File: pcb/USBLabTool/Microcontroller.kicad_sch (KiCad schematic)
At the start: 19 parts, among them J1 Conn_01x06_Pin, J2 Conn_02x12_Odd_Even, SW1 TS02-66-73-BK-100-SCR-D, U12 STM32H562VGTx, Y1 32.768kHz, Y2 NX2016SA-25M-EXS00A-CS08742

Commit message: fixes
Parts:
- added JP6, JP7: SJ, Jumper:SolderJumper-2_P1.3mm_Open_RoundedPad1.0x1.5mm, symbol Jumper:SolderJumper_2_Open
- added R82, R83: 0, Resistor_SMD:R_0603_1608Metric_Pad0.98x0.95mm_HandSolder, symbol Device:R
- added R84, R85: 5.1k, Resistor_SMD:R_0603_1608Metric_Pad0.98x0.95mm_HandSolder, symbol Device:R
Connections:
- net RCC_OSC32_IN: now also R82.1; no longer C35.2, Y1.2
- net RCC_OSC32_OUT: now also R83.1; no longer C36.2, Y1.1
- net RCC_OSC_IN: now also JP6.1 (A); no longer C33.1, Y2.1
- net RCC_OSC_OUT: now also JP7.2 (B); no longer C34.2, Y2.3
- net UCPD_CC1: now also R84.2; no longer U12.52 (PB13)
- net UCPD_CC2: now also R85.2; no longer U12.53 (PB14)
- net USB_D+ renamed USB_FS_P
- net USB_D- renamed USB_FS_N
- new net: R85.1, U12.53 (PB14)
- new net: C34.2, JP7.1 (A), Y2.3
- new net: C33.1, JP6.2 (B), Y2.1
- new net: C36.2, R83.2, Y1.1
- new net: C35.2, R82.2, Y1.2
- new net: R84.1, U12.52 (PB13)
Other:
- moved on the sheet: C35, C36, Y1

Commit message: V2 fixed
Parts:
- added JP8, JP9: SJ, Jumper:SolderJumper-2_P1.3mm_Open_RoundedPad1.0x1.5mm, symbol Jumper:SolderJumper_2_Open
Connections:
- net RCC_OSC32_IN: now also JP8.1 (A); no longer R82.1
- net RCC_OSC32_OUT: now also JP9.1 (A); no longer R83.1
- new net: JP9.2 (B), R83.1
- new net: JP8.2 (B), R82.1
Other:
- moved on the sheet: R83

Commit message: PCB V2 updates
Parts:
- removed CR2: ESDALC6V1-1U2, userfp:DIODE_ESDALC6V1-1U2_STM, symbol USBLabTool:ESDALC6V1-1U2
- removed JP8, JP9: SJ, Jumper:SolderJumper-2_P1.3mm_Open_RoundedPad1.0x1.5mm, symbol Jumper:SolderJumper_2_Open
- removed U12: STM32H562VGTx, Package_QFP:LQFP-100_14x14mm_P0.5mm, symbol MCU_ST_STM32H5:STM32H562VGTx
- added CR1: ESDALC6V1-1M2, Diode_SMD:D_SOD-882, symbol USBLabTool:ESDALC6V1-1M2
- added H3, H4: MountingHole, MountingHole:MountingHole_2.2mm_M2, symbol Mechanical:MountingHole
- added U12: STM32H563VITx, Package_QFP:LQFP-100_14x14mm_P0.5mm, symbol MCU_ST_STM32H5:STM32H563VITx
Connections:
- net +3.3V: now also U12.100 (VDD), U12.11 (VDD), U12.28 (VDD), U12.50 (VDD), U12.6 (VBAT), U12.73 (VDDUSB), U12.75 (VDD)
- net ADC1_INP0: now also U12.23 (PA0)
- net ADC2_INP3: now also U12.31 (PA6)
- net C0_IN: now also U12.29 (PA4)
- net C1_IN: now also U12.30 (PA5)
- net CH0_ACDC: now also U12.18 (PC3)
- net CH0_amp_1: now also U12.36 (PB1)
- net CH0_amp_10: now also U12.37 (PB2)
- net CH0_amp_2.5: now also U12.44 (PE13)
- net CH0_amp_5: now also U12.43 (PE12)
- net CH0_attenuate: now also U12.17 (PC2)
- net CH1_ACDC: now also U12.33 (PC4)
- net CH1_amp_1: now also U12.34 (PC5)
- net CH1_amp_10: now also U12.35 (PB0)
- net CH1_amp_2.5: now also U12.16 (PC1)
- net CH1_amp_5: now also U12.15 (PC0)
- net CH1_attenuate: now also U12.1 (PE2)
- net DEBUG_JTCK_SWCLK: now also U12.76 (PA14(JTCK)
- net DEBUG_JTD-SW0: now also U12.89 (PB3(JTDO)
- net DEBUG_JTMS-SWDI0: now also U12.72 (PA13(JTMS)
- net GAIN_C0: now also U12.64 (PC7)
- net GAIN_C1: now also U12.63 (PC6)
- net GND: now also CR1.2 (A), U12.10 (VSS), U12.27 (VSS), U12.49 (VSS), U12.74 (VSS), U12.99 (VSS)
- net GNDA: now also U12.19 (VSSA), U12.20 (VREF-)
- net LOGIC_IN0: now also U12.81 (PD0)
- net LOGIC_IN1: now also U12.82 (PD1)
- net LOGIC_IN10: now also U12.60 (PD13)
- net LOGIC_IN11: now also U12.59 (PD12)
- net LOGIC_IN12: now also U12.58 (PD11)
- net LOGIC_IN13: now also U12.57 (PD10)
- net LOGIC_IN14: now also U12.56 (PD9)
- net LOGIC_IN15: now also U12.55 (PD8)
- net LOGIC_IN2: now also U12.83 (PD2)
- net LOGIC_IN3: now also U12.84 (PD3)
- net LOGIC_IN4: now also U12.85 (PD4)
- net LOGIC_IN5: now also U12.86 (PD5)
- net LOGIC_IN6: now also U12.87 (PD6)
- net LOGIC_IN7: now also U12.88 (PD7)
- net LOGIC_IN8: now also U12.62 (PD15)
- net LOGIC_IN9: now also U12.61 (PD14)
- net NRST: now also CR1.1 (K), U12.14 (NRST)
- net RCC_OSC32_IN: now also R82.1, U12.8 (PC14)
- net RCC_OSC32_OUT: now also R83.1, U12.9 (PC15)
- net RCC_OSC_IN: now also U12.12 (PH0)
- net RCC_OSC_OUT: now also U12.13 (PH1)
- net TIM1_CH1: now also U12.67 (PA8)
- net TIM1_CH2: now also U12.69 (PA10)
- net TIM2_CH2: now also U12.24 (PA1)
- net TIM2_CH3: now also U12.25 (PA2)
- net UCPD_FLT: now also U12.66 (PC9)
- net USCPD_DBn: now also U12.68 (PA9)
- net VREFP: now also U12.21 (VREF+)
- net at C31.1, C32.1: now also U12.98 (VCAP)
- net at C31.2, C32.2: now also U12.48 (VCAP)
- net at R85.1: now also U12.53 (PB14)
- net at R54.2, R55.2: now also U12.22 (VDDA)
- net at R84.1: now also U12.52 (PB13)
- net at R53.2: now also U12.94 (BOOT0)
- new net USB_D+: U12.71 (PA12)
- new net USB_D-: U12.70 (PA11)
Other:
- moved on the sheet: R83

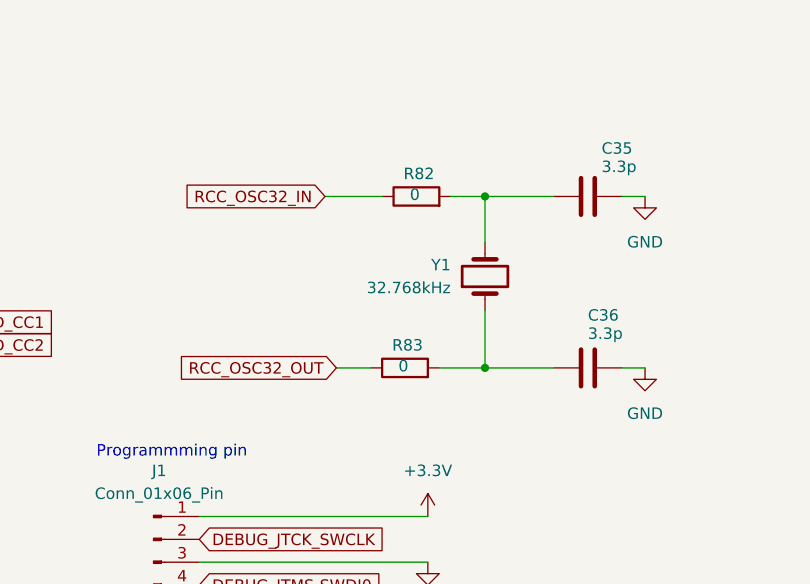
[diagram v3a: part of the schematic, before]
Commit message: add pads for 32kHz crystal
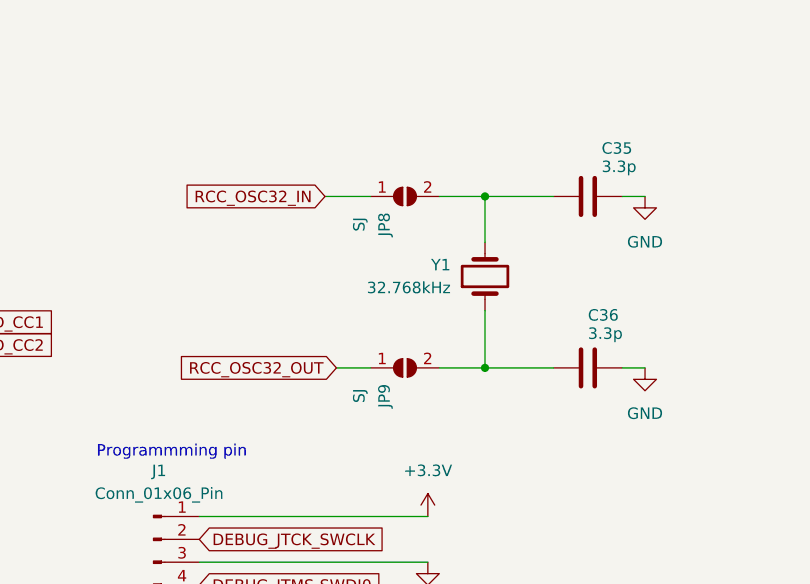
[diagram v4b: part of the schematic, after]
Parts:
- removed R82, R83: 0, Resistor_SMD:R_0603_1608Metric_Pad0.98x0.95mm_HandSolder, symbol Device:R
- added JP8, JP9: SJ, Jumper:SolderJumper-2_P1.3mm_Open_RoundedPad1.0x1.5mm, symbol Jumper:SolderJumper_2_Open
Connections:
- net RCC_OSC32_IN: now also JP8.1 (A)
- net RCC_OSC32_OUT: now also JP9.1 (A)
- net at C36.2, Y1.1: now also JP9.2 (B)
- net at C35.2, Y1.2: now also JP8.2 (B)
